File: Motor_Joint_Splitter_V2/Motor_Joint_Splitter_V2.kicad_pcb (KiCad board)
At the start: 2 copper layers, 40 x 40 mm, 30 parts, among them J1 Conn_01x08, J2 54602-908LF, J4 26605030, J7 Conn_01x05, U1 74ACT244MTCX

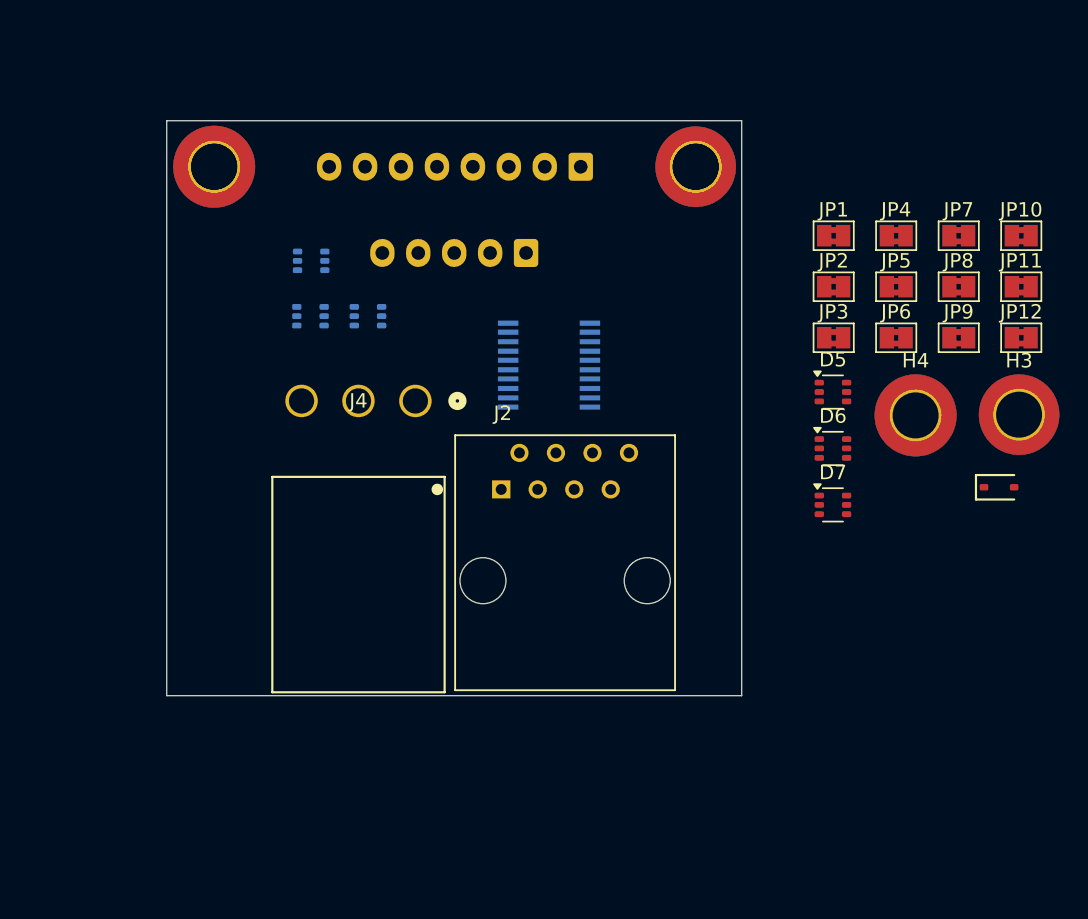
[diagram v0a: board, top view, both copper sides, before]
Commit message: Finished the first version of the new splitter PCB.
TODO:
- Update connectors to IDCs if we can find some 5 pin and 8 pin ones.
- Add part numbers for LCSC fields.
- Generate bill of materials.
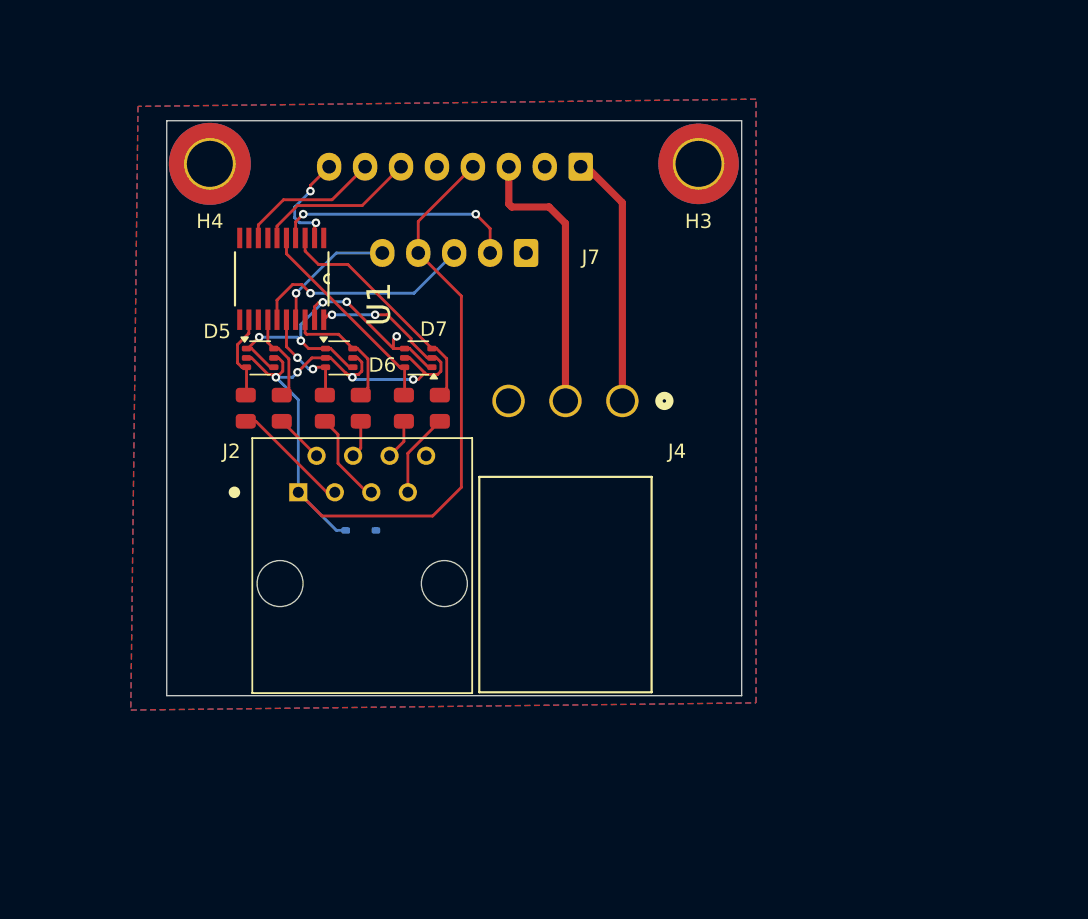
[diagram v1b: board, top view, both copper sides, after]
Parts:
- removed ? (x2): , 
- removed D1, D2, D3: BAT54SDW, Package_TO_SOT_SMD:SOT-363_SC-70-6
- removed the H3 at (239.3, 80.5)
- removed the H3 at (216.8, 63.2)
- removed the H4 at (183.3, 63.2)
- removed the H4 at (232.1, 80.5)
- removed JP1, JP10, JP11, JP12, JP2, JP3, JP4, JP5, JP6, JP7, JP8, JP9: SolderJumper_2_Bridged, Jumper:SolderJumper-2_P1.3mm_Bridged2Bar_Pad1.0x1.5mm
- added H3: MountingHole_Pad, MountingHole:MountingHole_3.2mm_M3_DIN965_Pad_TopBottom, F.Cu at (217.0, 63.0)
- added H4: MountingHole_Pad, MountingHole:MountingHole_3.2mm_M3_ISO7380_Pad_TopBottom, F.Cu at (183.0, 63.0)
- added R13: 120Ω, PCM_JLCPCB:R_0805, F.Cu at (185.5, 80.0)
- added R14: 120Ω, PCM_JLCPCB:R_0805, F.Cu at (193.5, 80.0)
- added R15: 120Ω, PCM_JLCPCB:R_0805, F.Cu at (196.5, 80.0)
- added R16: 120Ω, PCM_JLCPCB:R_0805, F.Cu at (199.0, 80.0)
- added R17: 120Ω, PCM_JLCPCB:R_0805, F.Cu at (191.0, 80.0)
- added R19: 120Ω, PCM_JLCPCB:R_0805, F.Cu at (188.0, 80.0)
- D4: moved to B.Cu
- U1: moved to F.Cu
- moved D4 44.5 mm to (193.5, 88.5), turned to 180 degrees
- moved D5 39.9 mm to (186.5, 76.5)
- moved D6 34.9 mm to (192.0, 76.5)
- moved D7 30.6 mm to (197.5, 76.5), turned to 180 degrees
- moved U1 19.5 mm to (188.0, 71.0), turned to -90 degrees
- moved J4 14.4 mm to (211.7, 79.5)
- moved J2 14.1 mm to (193.6, 92.2)
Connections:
- D5 pad 3: Net-(D5C-K) -> /C_B_Out
- D5 pad 6: Net-(D5A-K) -> /C_A_Out
- D6 pad 3: Net-(D6C-K) -> /SEA_I_Out
- D6 pad 6: Net-(D6A-K) -> /C_I_Out
- D7 pad 3: Net-(D7C-K) -> /SEA_B_Out
- D7 pad 6: Net-(D7A-K) -> /SEA_A_Out
- J2 pad 2: /C_A_Out -> /C_A_Out_2
- J2 pad 3: /C_B_Out -> /C_B_Out_2
- J2 pad 4: /C_I_Out -> /C_I_Out_2
- J2 pad 5: /SEA_I_Out -> /SEA_I_Out_2
- J2 pad 6: /SEA_A_Out -> /SEA_A_Out_2
- J2 pad 7: /SEA_B_Out -> /SEA_B_Out_2
- U1 pad 12: /SEA_A_Out -> /C_B_Out
- U1 pad 14: /C_I_Out -> /C_A_Out
- U1 pad 15: /SEA_I -> /SEA_A
- U1 pad 16: /C_B_Out -> /SEA_I_Out
- U1 pad 18: /C_A_Out -> /C_I_Out
- U1 pad 2: /C_A -> /C_I
- U1 pad 4: /C_B -> /SEA_I
- U1 pad 5: /SEA_I_Out -> /SEA_A_Out
- U1 pad 6: /C_I -> /C_A
- U1 pad 8: /SEA_A -> /C_B
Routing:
- net +5V: track 0.00 -> 84.0 mm, vias 0 -> 6
- net GND: track 0.00 -> 26.4 mm, vias 0 -> 5
- net /Cos: track 0.00 -> 19.4 mm
- net /Sin: track 0.00 -> 17.7 mm
- net /SEA_I: track 0.00 -> 17.0 mm, vias 0 -> 2
- net /SEA_B_Out: track 0.00 -> 16.6 mm
- net /SEA_A: track 0.00 -> 15.6 mm, vias 0 -> 1
- net /SEA_A_Out: track 0.00 -> 14.6 mm
- net /C_A: track 0.00 -> 11.2 mm
- net /C_B: track 0.00 -> 10.0 mm
- net /SEA_B: track 0.00 -> 9.02 mm, vias 0 -> 1
- net /C_I_Out: track 0.00 -> 8.76 mm
- net /C_B_Out_2: track 0.00 -> 8.24 mm
- net /C_I: track 0.00 -> 7.26 mm, vias 0 -> 2
- net /SEA_I_Out: track 0.00 -> 7.26 mm, vias 0 -> 2
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- added copper zone on B.Cu, net GND
- added copper zone on F.Cu, net GND

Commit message: Still a work in progress. The molex connectors used by the USM motors are surface mounts, looking for compatible through-hole headers instead.
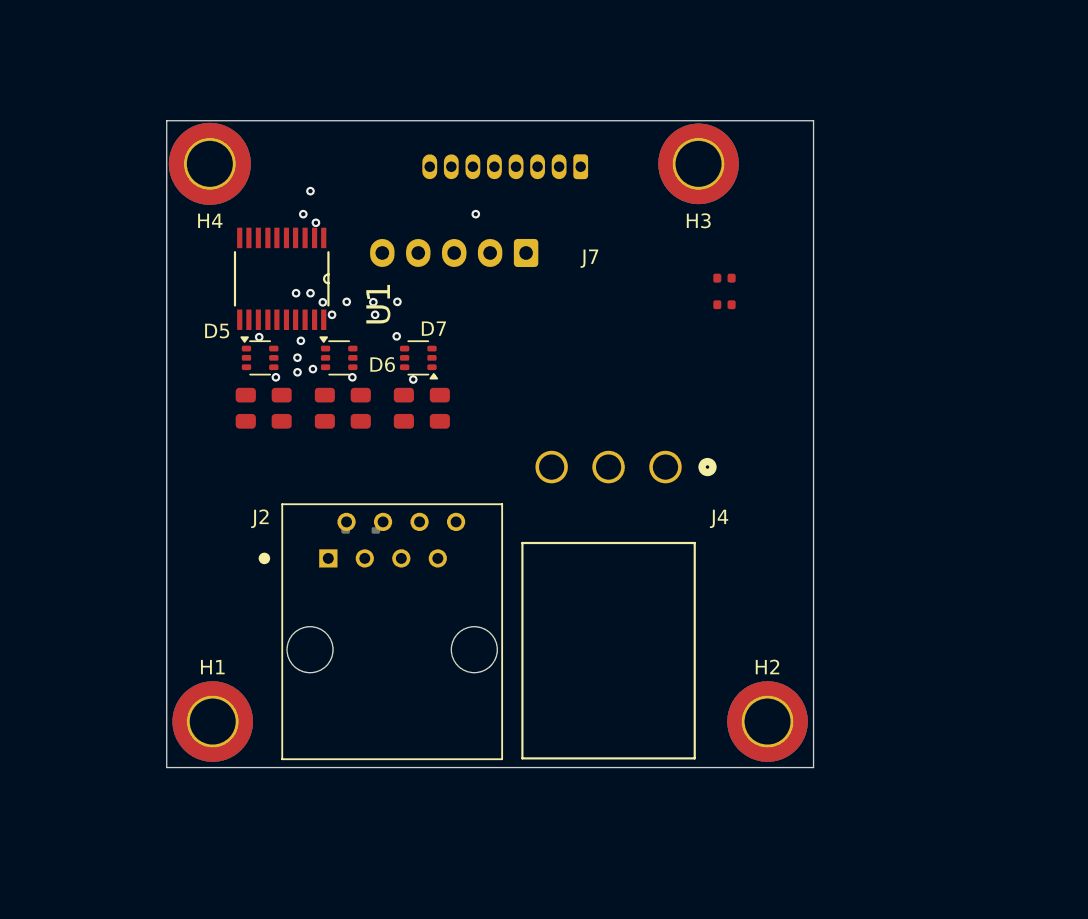
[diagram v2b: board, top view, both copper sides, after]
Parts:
- added C1: 1uF, PCM_JLCPCB:C_0402, F.Cu at (218.8, 71.0)
- added C2: 1uF, PCM_JLCPCB:C_0402, F.Cu at (218.8, 72.8)
- added H1: MountingHole_Pad, MountingHole:MountingHole_3.2mm_M3_DIN965_Pad_TopBottom, F.Cu at (183.2, 101.8)
- added H2: MountingHole_Pad, MountingHole:MountingHole_3.2mm_M3_DIN965_Pad_TopBottom, F.Cu at (221.8, 101.8)
- J1: footprint Connector_JST:JST_XH_B8B-XH-A_1x08_P2.50mm_Vertical -> Connector_JST:JST_ZH_B8B-ZR_1x08_P1.50mm_Vertical
- moved J4 5.49 mm to (214.7, 84.1)
- moved J2 5.05 mm to (195.7, 96.8)
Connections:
- U1 pad 11: unconnected-(U1-I7-Pad11) -> GND
- U1 pad 13: unconnected-(U1-I6-Pad13) -> GND
- U1 pad 7: unconnected-(U1-O6-Pad7) -> GND
- U1 pad 9: unconnected-(U1-O7-Pad9) -> GND
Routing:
- net +5V: track 84.0 -> 0.00 mm, vias 6 -> 8
- net GND: track 26.4 -> 0.00 mm
- net /Cos: track 19.4 -> 0.00 mm
- net /Sin: track 17.7 -> 0.00 mm
- net /SEA_I: track 17.0 -> 0.00 mm, vias 2 -> 1
- net /SEA_B_Out: track 16.6 -> 0.00 mm
- net /SEA_A: track 15.6 -> 0.00 mm
- net /SEA_A_Out: track 14.6 -> 0.00 mm
- net /C_A: track 11.2 -> 0.00 mm, vias 0 -> 1
- net /C_B: track 10.0 -> 0.00 mm
- net /SEA_B: track 9.02 -> 0.00 mm
- net /C_I_Out: track 8.76 -> 0.00 mm
- net /C_B_Out_2: track 8.24 -> 0.00 mm
- net /C_I: track 7.26 -> 0.00 mm
- net /SEA_I_Out: track 7.26 -> 0.00 mm
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- removed copper zone on B.Cu, net GND
- removed copper zone on F.Cu, net GND
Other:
- board size 40 x 40 mm -> 45 x 45 mm

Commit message: Added a new motor connector that might work on our board. Need to see if we can install it ourselves.
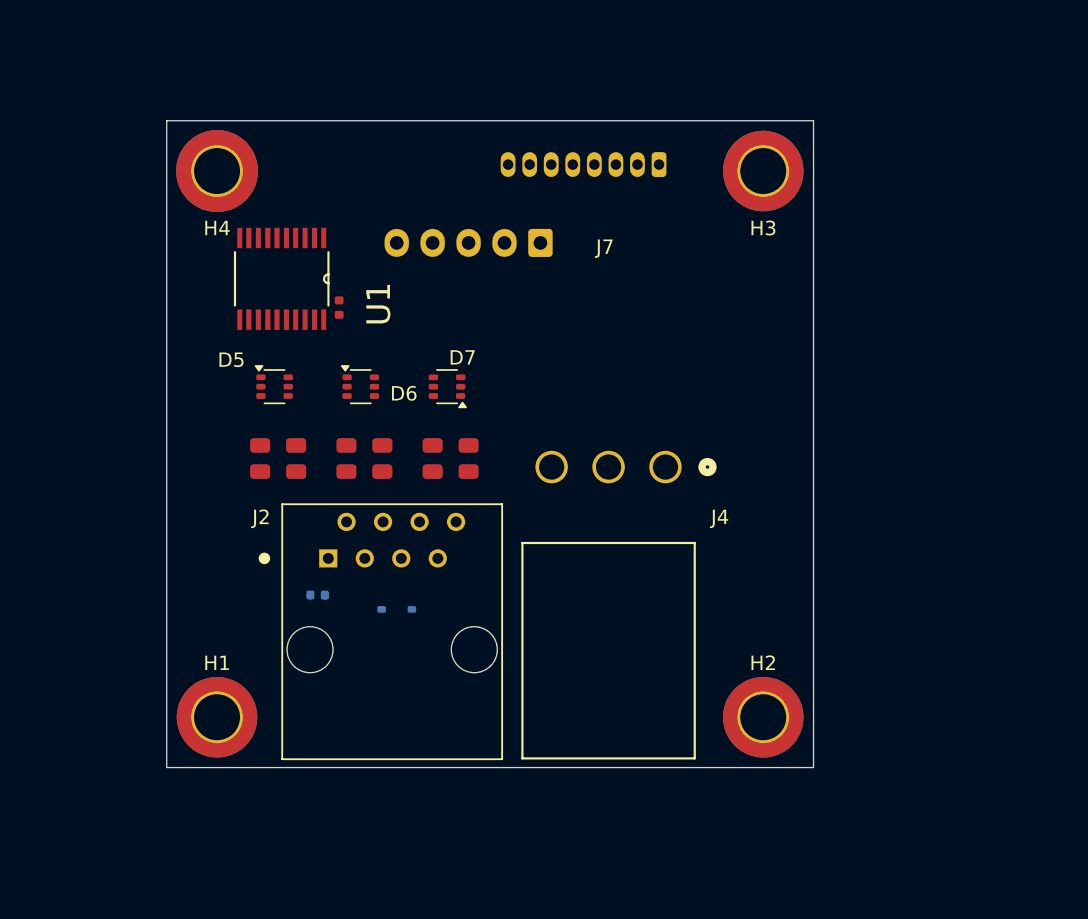
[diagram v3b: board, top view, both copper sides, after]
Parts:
- C2: moved to B.Cu
- moved C2 34.8 mm to (190.5, 93.0)
- moved C1 26.9 mm to (192.0, 73.0), turned to 90 degrees
- moved D4 6.04 mm to (196.0, 94.0)
- moved J1 5.45 mm to (214.2, 63.0)
- moved H3 4.53 mm to (221.5, 63.5)
- moved R15 4.03 mm to (198.5, 83.5)
- moved R16 4.03 mm to (201.0, 83.5)
- moved R14 3.81 mm to (195.0, 83.5)
- moved R17 3.81 mm to (192.5, 83.5)
- moved R13 3.64 mm to (186.5, 83.5)
- moved R19 3.64 mm to (189.0, 83.5)
- moved D7 2.83 mm to (199.5, 78.5)
- moved D6 2.50 mm to (193.5, 78.5)
- moved D5 2.24 mm to (187.5, 78.5)
- moved J7 1.22 mm to (206.0, 68.5)
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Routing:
- net GND: vias 5 -> 0
- net /SEA_I_Out: vias 2 -> 0
- net /SEA_I: vias 1 -> 0
- net /SEA_B: vias 1 -> 0
- net /SEA_A: vias 1 -> 0
- net /C_I: vias 2 -> 0
- net /C_A: vias 1 -> 0
- net +5V: vias 8 -> 0

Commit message: Updated the PCB design and library for added parts.
Need to find pre-crimped wires for making the female-to-female 5-pin connector. Outside of that, everything else that's already picked should work fine.
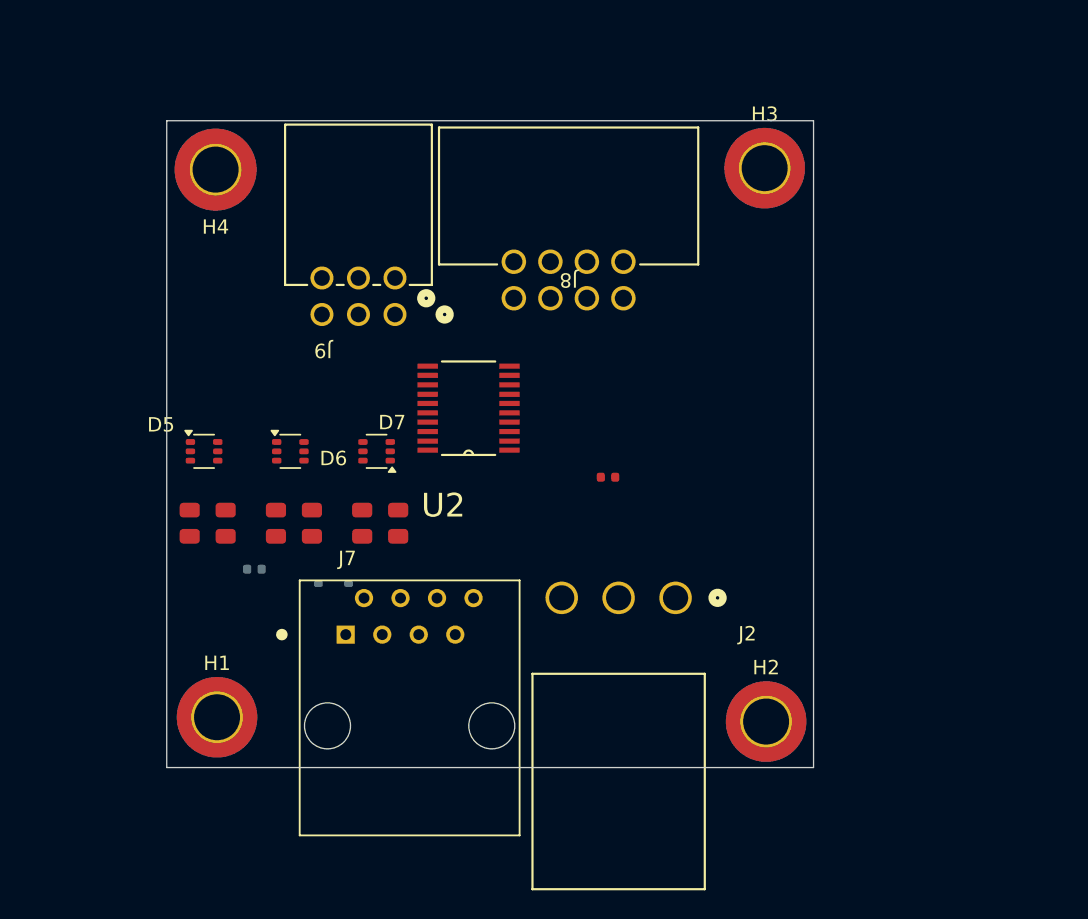
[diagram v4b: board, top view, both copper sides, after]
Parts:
- removed C1: 1uF, PCM_JLCPCB:C_0402
- removed J1: Conn_01x08, Connector_JST:JST_ZH_B8B-ZR_1x08_P1.50mm_Vertical
- removed J4: 26605030, motor_power_connector:CONN_SDA-41792_M450_03_MOL
- removed U1: 74ACT244MTCX, line_driver:SOP65P640X120-20N
- added C4: 1uF, PCM_JLCPCB:C_0402, F.Cu at (210.7, 84.8)
- added J8: molex_conn_2x4_P2.54_702470851, splitter_parts:CONN_7024708xx_MOL, F.Cu at (204.2, 72.4)
- added J9: molex_conn_2x3_P2.54_901303106, splitter_parts:CONN_SDA-90130_RA_06_MOL, F.Cu at (195.9, 73.5)
- added U2: 74ACT244MTCX, splitter_parts:line_driver_SOP65P640X120-20N, F.Cu at (201.0, 80.0)
- J2: value 54602-908LF -> 26605030; footprint ethernet_connector:AMPHENOL_54602-908LF -> splitter_parts:CONN_SDA-41792_M450_03_MOL
- J7: value Conn_01x05 -> ethernet_54602-908LF; footprint Connector_JST:JST_EH_B5B-EH-A_1x05_P2.50mm_Vertical -> splitter_parts:AMPHENOL_54602-908LF; moved to F.Cu
- moved J7 34.8 mm to (196.9, 102.1), turned to 0 degrees
- moved J2 20.0 mm to (215.4, 93.2)
- moved D5 6.65 mm to (182.6, 83.0)
- moved D6 6.65 mm to (188.6, 83.0)
- moved D7 6.65 mm to (194.6, 83.0)
- moved R13 6.65 mm to (181.6, 88.0)
- moved R14 6.65 mm to (190.1, 88.0)
- moved R15 6.65 mm to (193.6, 88.0)
- moved R16 6.65 mm to (196.1, 88.0)
- moved R17 6.65 mm to (187.6, 88.0)
- moved R19 6.65 mm to (184.1, 88.0)
- moved C2 4.75 mm to (186.1, 91.2)
- moved D4 4.75 mm to (191.6, 92.2)
- moved H2 0.36 mm to (221.7, 101.8)
- moved H3 0.22 mm to (221.6, 63.3)
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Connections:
- J2 pad 1: +5V -> /Sin
- J2 pad 2: /C_A_Out_2 -> /Cos
- J2 pad 3: /C_B_Out_2 -> GND
- J7 pad 1: GND -> +5V
- J7 pad 2: /SEA_I -> /C_A_Out_2
- J7 pad 3: /SEA_A -> /C_B_Out_2
- J7 pad 4: +5V -> /C_I_Out_2
- J7 pad 5: /SEA_B -> /SEA_I_Out_2

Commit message: Updated the headers, should all be good now. Need to double check the routing to make sure it's not going to be an issue.
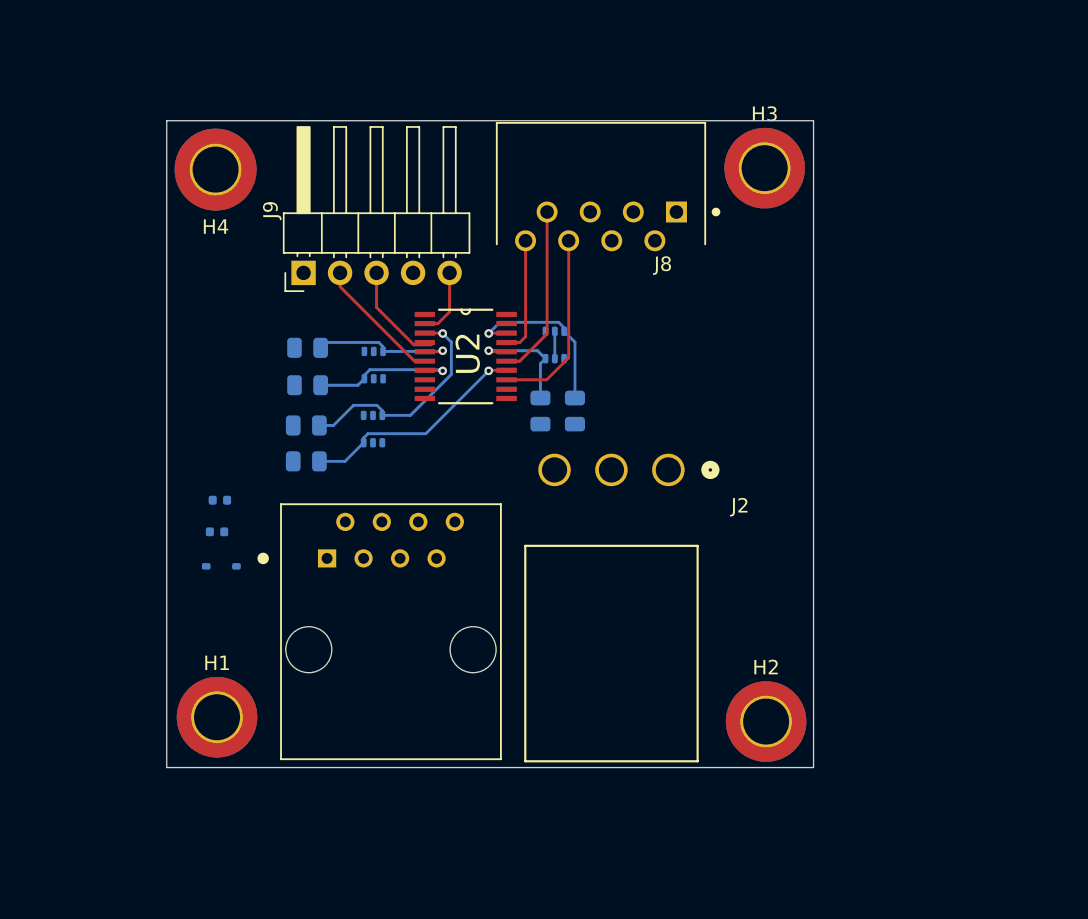
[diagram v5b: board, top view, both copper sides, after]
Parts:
- C4, D5, D6, D7, R13, R14, R15, R16, R17, R19: moved to B.Cu
- J8: value molex_conn_2x4_P2.54_702470851 -> motor_connector_292206-8; footprint splitter_parts:CONN_7024708xx_MOL -> splitter_parts:TE_292206-8
- J9: value molex_conn_2x3_P2.54_901303106 -> Conn_01x05; footprint splitter_parts:CONN_SDA-90130_RA_06_MOL -> Connector_PinHeader_2.54mm:PinHeader_1x05_P2.54mm_Horizontal
- moved C4 27.0 mm to (183.7, 86.4)
- moved R13 14.7 mm to (189.8, 75.8), turned to 180 degrees
- moved R15 14.6 mm to (206.0, 80.2)
- moved R16 14.6 mm to (208.4, 80.2)
- moved D7 14.4 mm to (207.0, 75.6), turned to -90 degrees
- moved D5 13.2 mm to (194.4, 77.0), turned to -90 degrees
- moved R19 11.2 mm to (189.8, 78.4), turned to 180 degrees
- moved J2 8.91 mm to (214.9, 84.3)
- moved D4 7.89 mm to (183.8, 91.0), turned to 0 degrees
- moved J8 7.86 mm to (210.2, 67.3)
- moved J9 6.99 mm to (189.5, 70.6), turned to 90 degrees
- moved R14 6.81 mm to (189.7, 81.2), turned to 180 degrees
- moved D6 5.96 mm to (194.3, 81.5), turned to 90 degrees
- moved J7 5.46 mm to (195.6, 96.8)
- moved R17 4.79 mm to (189.7, 83.7), turned to 180 degrees
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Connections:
- J8 pad 1: /C_I -> /Sin
- J8 pad 2: /C_B -> GND
- J8 pad 3: /C_A -> /Cos
- J8 pad 4: GND -> +5V
- J8 pad 5: +5V -> GND
- J8 pad 6: /Cos -> /C_A
- J8 pad 7: GND -> /C_B
- J8 pad 8: /Sin -> /C_I
- J9 pad 1: /SEA_B -> GND
- J9 pad 2: +5V -> /SEA_I
- J9 pad 3: /SEA_I -> /SEA_A
- J9 pad 4: /SEA_A -> +5V
- J9 pad 5: GND -> /SEA_B
- U2 pad 12: /C_B_Out -> GND
- U2 pad 13: GND -> /C_A
- U2 pad 14: /C_A_Out -> /SEA_I_Out
- U2 pad 15: /SEA_A -> /C_B
- U2 pad 16: /SEA_I_Out -> /SEA_A_Out
- U2 pad 17: /SEA_B -> /C_I
- U2 pad 18: /C_I_Out -> /SEA_B_Out
- U2 pad 2: /C_I -> /SEA_B
- U2 pad 3: /SEA_B_Out -> /C_I_Out
- U2 pad 4: /SEA_I -> /SEA_A
- U2 pad 5: /SEA_A_Out -> /C_B_Out
- U2 pad 6: /C_A -> /SEA_I
- U2 pad 7: GND -> /C_A_Out
- U2 pad 8: /C_B -> GND
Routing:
- net /SEA_I_Out: track 0.00 -> 15.8 mm, vias 0 -> 1
- net /C_I_Out: track 0.00 -> 15.8 mm, vias 0 -> 1
- net /C_A: track 0.00 -> 13.1 mm
- net /SEA_B_Out: track 0.00 -> 12.2 mm, vias 0 -> 1
- net /C_B: track 0.00 -> 12.1 mm
- net /C_B_Out: track 0.00 -> 10.4 mm, vias 0 -> 1
- net /C_A_Out: track 0.00 -> 10.4 mm, vias 0 -> 1
- net /SEA_I: track 0.00 -> 9.00 mm
- net /SEA_A_Out: track 0.00 -> 8.34 mm, vias 0 -> 1
- net /C_I: track 0.00 -> 8.16 mm
- net /SEA_A: track 0.00 -> 7.28 mm
- net /SEA_B: track 0.00 -> 4.78 mm
- net +5V: track 0.00 -> 1.90 mm
